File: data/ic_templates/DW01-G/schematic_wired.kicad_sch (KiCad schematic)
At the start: 12 parts, among them J1 B+/B-/P+/P-, Q1 FS8205A, U1 DW01-G

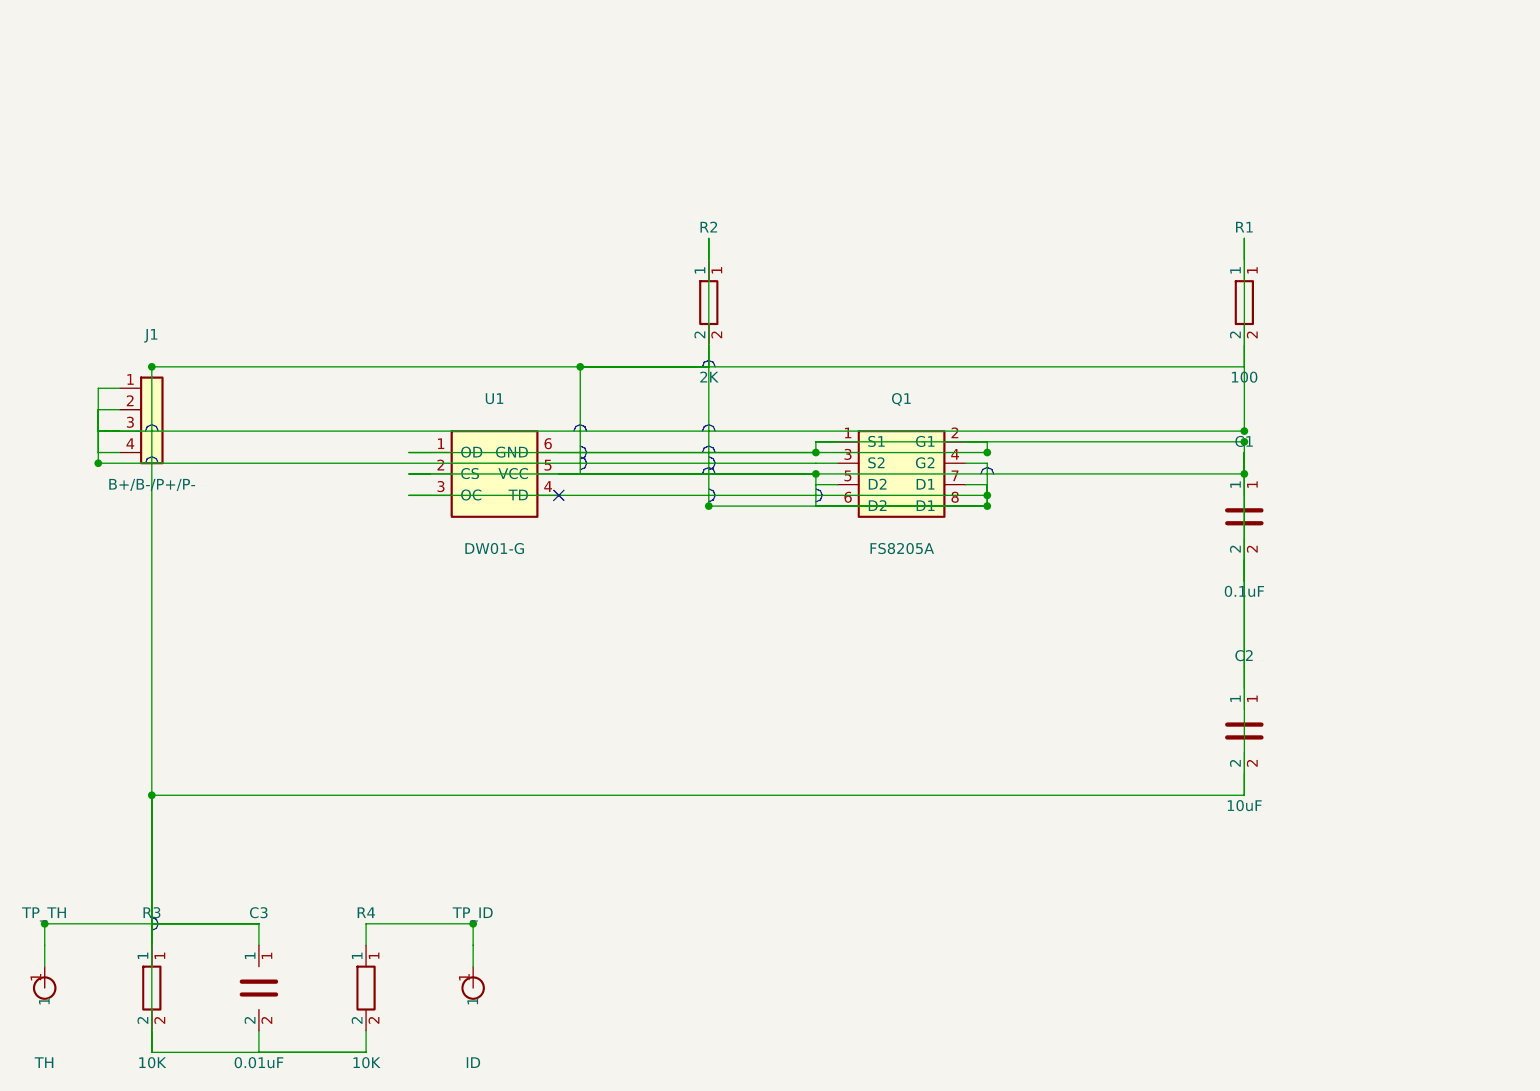
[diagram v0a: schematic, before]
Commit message: fix: 修复黑框检测阈值策略 — 固定阈值70改为 Otsu+Adaptive 混合阈值
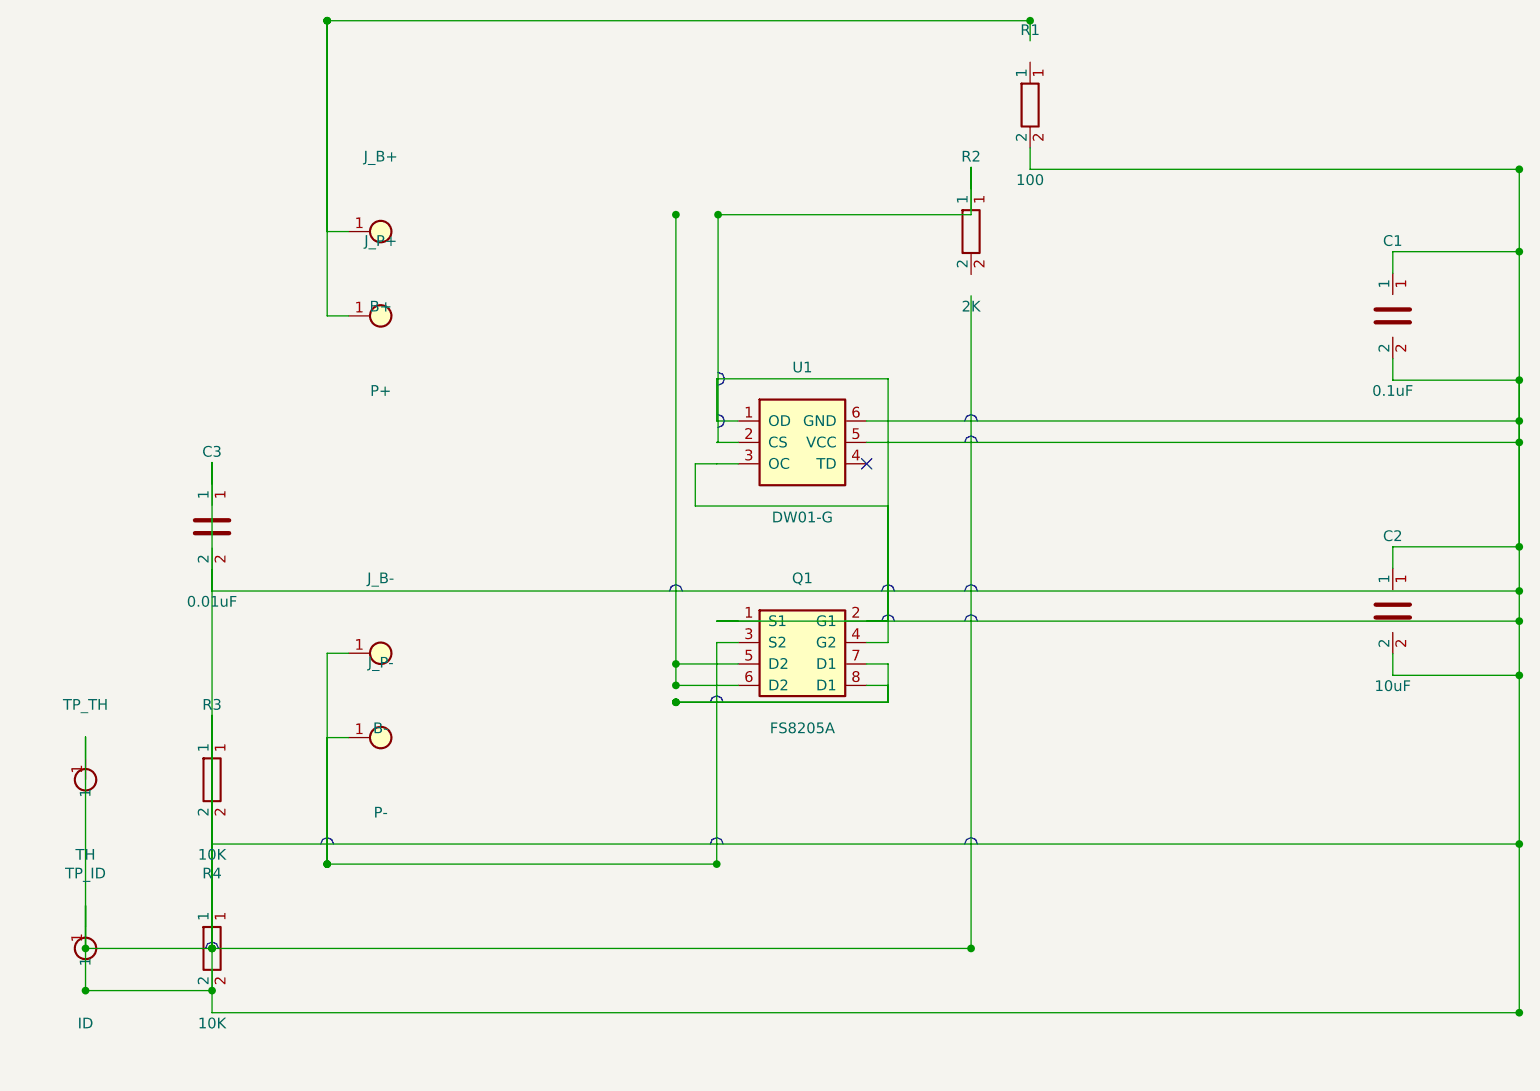
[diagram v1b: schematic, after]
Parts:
- removed J1: B+/B-/P+/P-, Connector_PinHeader_2.54mm:PinHeader_1x04_P2.54mm_Vertical, symbol battery_protection:Conn_01x04
- added J_B+: B+, Connector_PinHeader_2.54mm:PinHeader_1x01_P2.54mm_Vertical, symbol battery_protection:Conn_01x01
- added J_B-: B-, Connector_PinHeader_2.54mm:PinHeader_1x01_P2.54mm_Vertical, symbol battery_protection:Conn_01x01
- added J_P+: P+, Connector_PinHeader_2.54mm:PinHeader_1x01_P2.54mm_Vertical, symbol battery_protection:Conn_01x01
- added J_P-: P-, Connector_PinHeader_2.54mm:PinHeader_1x01_P2.54mm_Vertical, symbol battery_protection:Conn_01x01
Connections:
- net at C1.1, C1.2, C2.1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: now also R4.1, TP_ID.1; no longer Q1.3 (S2), Q1.5 (D2), Q1.6 (D2), Q1.7 (D1), Q1.8 (D1), R1.1, R2.1, R2.2, U1.2 (CS)
- new net: J_B+.1, J_P+.1
- new net: J_B-.1, J_P-.1, Q1.3 (S2)
- new net: R2.1, U1.2 (CS)
- new net: Q1.5 (D2), Q1.6 (D2)
- new net: Q1.7 (D1), Q1.8 (D1)
